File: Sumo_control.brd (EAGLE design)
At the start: 60 x 22.5 mm, 14 parts, among them X1 MICROMATCH-8

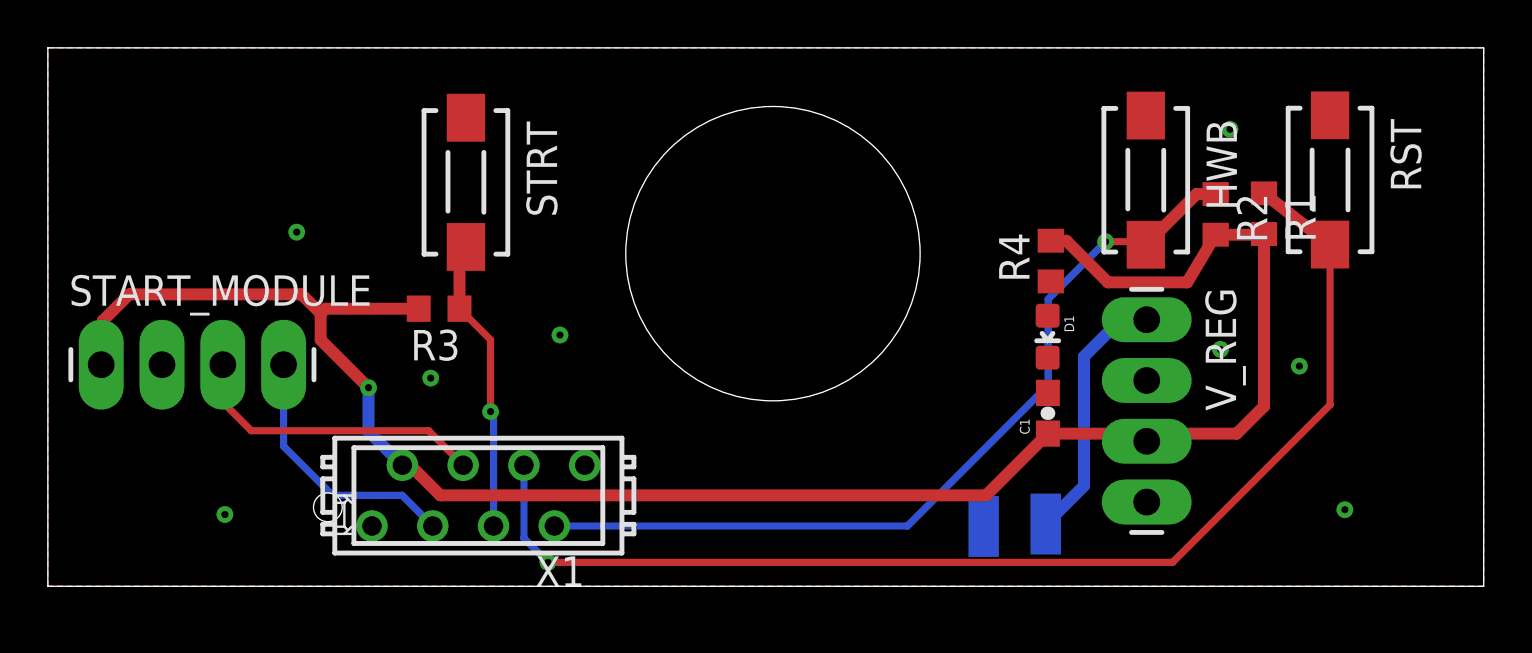
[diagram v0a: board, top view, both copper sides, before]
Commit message: Adjust control board to meet right EDC requirements
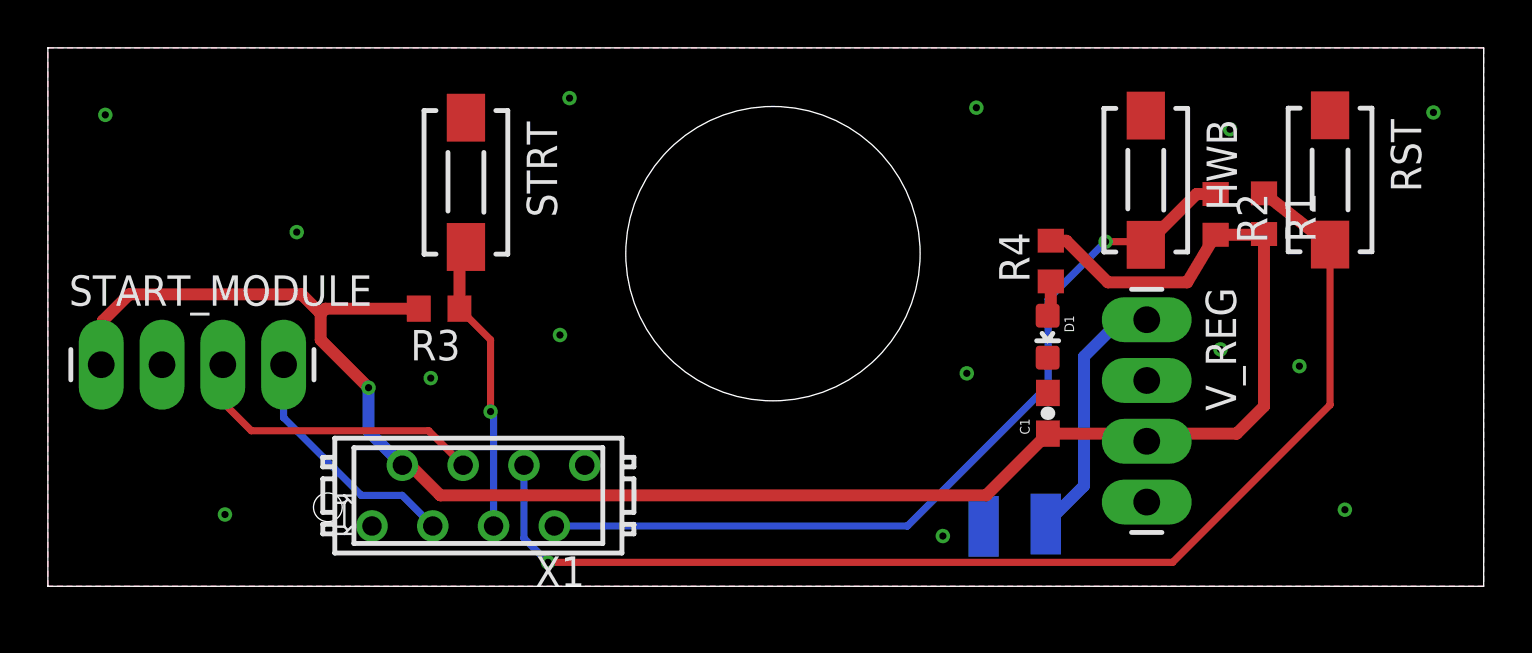
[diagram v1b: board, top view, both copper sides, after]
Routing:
- net N$1: track 0.00 -> 1.49 mm
- net KILL: track 11.0 -> 10.3 mm
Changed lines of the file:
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@@
 </class>
 </classes>
-<designrules name="default">
+<designrules name="SeeedStudio_2layer_DRU_modified">
 <description language="de">&lt;b&gt;EAGLE Design Rules&lt;/b&gt;
 &lt;p&gt;
@@
 necessary adjustments and save your customized
 design rules under a new name.</description>
+<description language="zh">&lt;b&gt;Seeed Studio EAGLE Design Rules&lt;/b&gt;
+</description>
 <param name="layerSetup" value="(1*16)"/>
-<param name="mtCopper" value="0.035mm 0.035mm 0.035mm 0.035mm 0.035mm 0.035mm 0.035mm 0.035mm 0.035mm 0.035mm 0.035mm 0.035mm 0.035mm 0.035mm 0.035mm 0.035mm"/>
-<param name="mtIsolate" value="1.5mm 0.15mm 0.2mm 0.15mm 0.2mm 0.15mm 0.2mm 0.15mm 0.2mm 0.15mm 0.2mm 0.15mm 0.2mm 0.15mm 0.2mm"/>
-<param name="mdWireWire" value="8mil"/>
-<param name="mdWirePad" value="8mil"/>
-<param name="mdWireVia" value="8mil"/>
-<param name="mdPadPad" value="8mil"/>
-<param name="mdPadVia" value="8mil"/>
-<param name="mdViaVia" value="8mil"/>
-<param name="mdSmdPad" value="8mil"/>
-<param name="mdSmdVia" value="8mil"/>
-<param name="mdSmdSmd" value="8mil"/>
+<param name="mtCopper" value="0.035mm 0.0175mm 0.035mm 0.035mm 0.035mm 0.035mm 0.035mm 0.035mm 0.035mm 0.035mm 0.035mm 0.035mm 0.035mm 0.035mm 0.0175mm 0.035mm"/>
+<param name="mtIsolate" value="1.5mm 1.1mm 0.2mm 0.15mm 0.2mm 0.15mm 0.2mm 0.15mm 0.2mm 0.15mm 0.2mm 0.15mm 0.2mm 0.15mm 0.2mm"/>
+<param name="mdWireWire" value="0.2mm"/>
+<param name="mdWirePad" value="0.2mm"/>
+<param name="mdWireVia" value="0.2mm"/>
+<param name="mdPadPad" value="0.2mm"/>
+<param name="mdPadVia" value="0.2mm"/>
+<param name="mdViaVia" value="0.2mm"/>
+<param name="mdSmdPad" value="0mil"/>
+<param name="mdSmdVia" value="0mil"/>
+<param name="mdSmdSmd" value="0mil"/>
 <param name="mdViaViaSameLayer" value="8mil"/>
 <param name="mnLayersViaInSmd" value="2"/>
-<param name="mdCopperDimension" value="40mil"/>
-<param name="mdDrill" value="8mil"/>
+<param name="mdCopperDimension" value="10mil"/>
+<param name="mdDrill" value="10mil"/>
 <param name="mdSmdStop" value="0mil"/>
-<param name="msWidth" value="10mil"/>
-<param name="msDrill" value="24mil"/>
-<param name="msMicroVia" value="9.99mm"/>
+<param name="msWidth" value="0.2mm"/>
+<param name="msDrill" value="0.3mm"/>
+<param name="msMicroVia" value="0.3mm"/>
 <param name="msBlindViaRatio" value="0.5"/>
 <param name="rvPadTop" value="0.25"/>
@@
 <param name="rlMinPadBottom" value="10mil"/>
 <param name="rlMaxPadBottom" value="20mil"/>
-<param name="rlMinViaOuter" value="8mil"/>
+<param name="rlMinViaOuter" value="6mil"/>
 <param name="rlMaxViaOuter" value="20mil"/>
-<param name="rlMinViaInner" value="8mil"/>
+<param name="rlMinViaInner" value="6mil"/>
 <param name="rlMaxViaInner" value="20mil"/>
 <param name="rlMinMicroViaOuter" value="4mil"/>
@@
 <param name="psTop" value="-1"/>
 <param name="psBottom" value="-1"/>
-<param name="psFirst" value="-1"/>
+<param name="psFirst" value="0"/>
 <param name="psElongationLong" value="100"/>
 <param name="psElongationOffset" value="100"/>
 <param name="mvStopFrame" value="1"/>
 <param name="mvCreamFrame" value="0"/>
-<param name="mlMinStopFrame" value="4mil"/>
-<param name="mlMaxStopFrame" value="4mil"/>
+<param name="mlMinStopFrame" value="2mil"/>
+<param name="mlMaxStopFrame" value="2mil"/>
 <param name="mlMinCreamFrame" value="0mil"/>
 <param name="mlMaxCreamFrame" value="0mil"/>
-<param name="mlViaStopLimit" value="0mil"/>
+<param name="mlViaStopLimit" value="100mil"/>
 <param name="srRoundness" value="0"/>
 <param name="srMinRoundness" value="0mil"/>
 <param name="srMaxRoundness" value="0mil"/>
-<param name="slThermalIsolate" value="10mil"/>
+<param name="slThermalIsolate" value="0.2mm"/>
 <param name="slThermalsForVias" value="0"/>
 <param name="dpMaxLengthDifference" value="10mm"/>
@@
 <param name="checkAngle" value="0"/>
 <param name="checkFont" value="1"/>
-<param name="checkRestrict" value="1"/>
+<param name="checkRestrict" value="0"/>
 <param name="useDiameter" value="13"/>
 <param name="maxErrors" value="50"/>
@@
 <via x="54.2" y="3.2" extent="1-16" drill="0.3"/>
 <via x="21.4" y="10.5" extent="1-16" drill="0.3"/>
+<via x="2.4" y="19.7" extent="1-16" drill="0.3"/>
+<via x="21.8" y="20.4" extent="1-16" drill="0.3"/>
+<via x="38.8" y="20" extent="1-16" drill="0.3"/>
+<via x="38.4" y="8.9" extent="1-16" drill="0.3"/>
+<via x="57.9" y="19.8" extent="1-16" drill="0.3"/>
+<via x="37.4" y="2.1" extent="1-16" drill="0.3"/>
 </signal>
 <signal name="HWB">
@@
 <contactref element="X1" pad="3"/>
 <wire x1="16.085" y1="2.52" x2="14.805" y2="3.8" width="0.3" layer="16"/>
-<wire x1="14.805" y1="3.8" x2="11.9" y2="3.8" width="0.3" layer="16"/>
-<wire x1="11.9" y1="3.8" x2="9.85" y2="5.85" width="0.3" layer="16"/>
-<wire x1="9.85" y1="5.85" x2="9.85" y2="9.26" width="0.3" layer="16"/>
+<wire x1="14.805" y1="3.8" x2="13.1" y2="3.8" width="0.3" layer="16"/>
+<wire x1="13.1" y1="3.8" x2="9.85" y2="7.05" width="0.3" layer="16"/>
+<wire x1="9.85" y1="7.05" x2="9.85" y2="9.26" width="0.3" layer="16"/>
 </signal>
 <signal name="START">
@@
 <contactref element="R4" pad="1"/>
 <contactref element="D1" pad="A"/>
-<wire x1="41.78" y1="11.307" x2="41.91" y2="12.74" width="0" layer="19" extent="1-1"/>
+<wire x1="41.78" y1="11.307" x2="41.91" y2="11.437" width="0.5" layer="1"/>
+<wire x1="41.91" y1="11.437" x2="41.91" y2="12.74" width="0.5" layer="1"/>
 </signal>
 </signals>
